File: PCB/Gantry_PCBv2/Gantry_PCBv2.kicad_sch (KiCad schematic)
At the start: 64 parts, among them J1 Conn_01x14, J10 B2B-XH-A_LF__SN_, J11 B2B-XH-A_LF__SN_, J12 B2B-XH-A_LF__SN_, J13 Conn_01x03_Pin, J14 USB_C_Receptacle_USB2.0_16P, J17 B2B-XH-A_LF__SN_, J2 Conn_01x14, J3 Conn_01x10, J4 Screw_Terminal_01x02, J5 DCJ200-10-A-XX-X_REVA, J6 Conn_01x04_Pin, J7 Conn_01x04_Pin, J8 Conn_01x04_Pin, J9 Conn_01x04_Pin, Q1 SS8050, Q2 SS8050, SW7 SW_0, SW8 SW_EN, U1 ESP32-WROOM-32E, U2 CH340C, U3 TB6612FNG H-bridge Motor Driv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, U4 LM2576S-5, U5 AMS1117-3.3, U6 DRV8825_STEPPER_MOTOR_DRIVER_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, U7 DRV8825_STEPPER_MOTOR_DRIVER_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, U8 DRV8825_STEPPER_MOTOR_DRIVER_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, U9 DRV8825_STEPPER_MOTOR_DRIVER_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

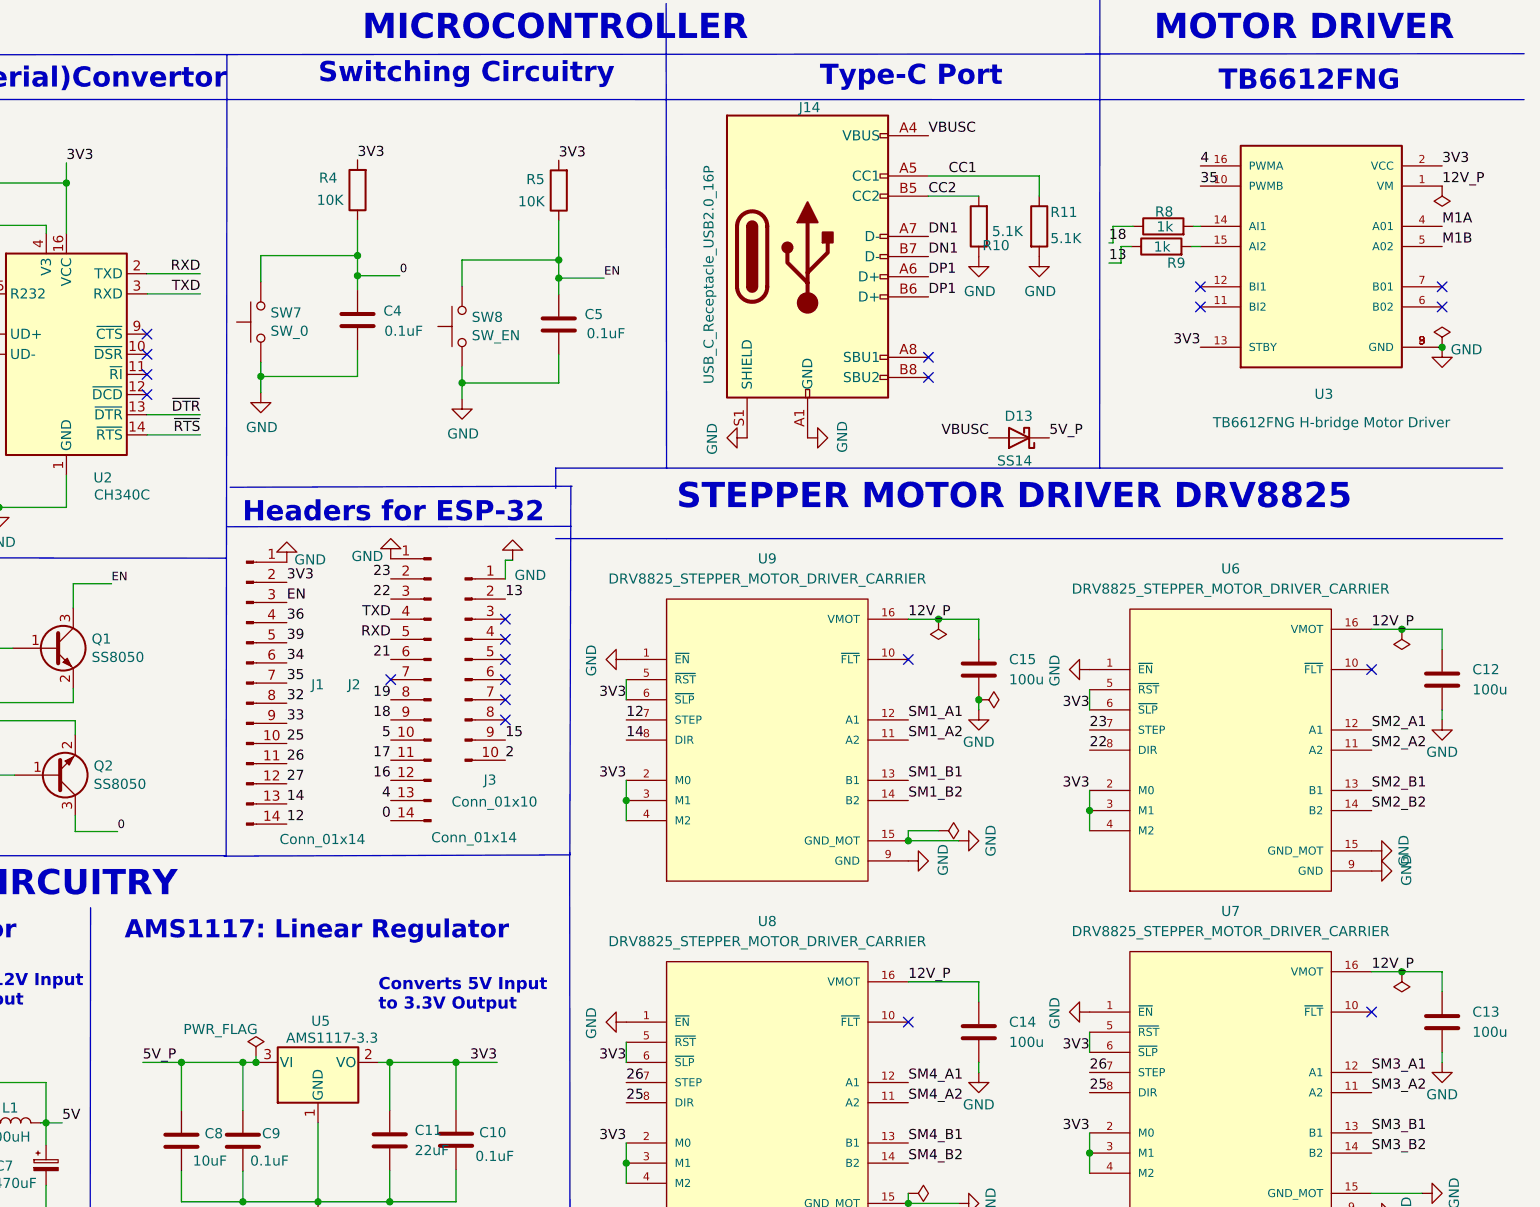
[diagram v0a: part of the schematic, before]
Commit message: final PCB Rounting without silkscreen
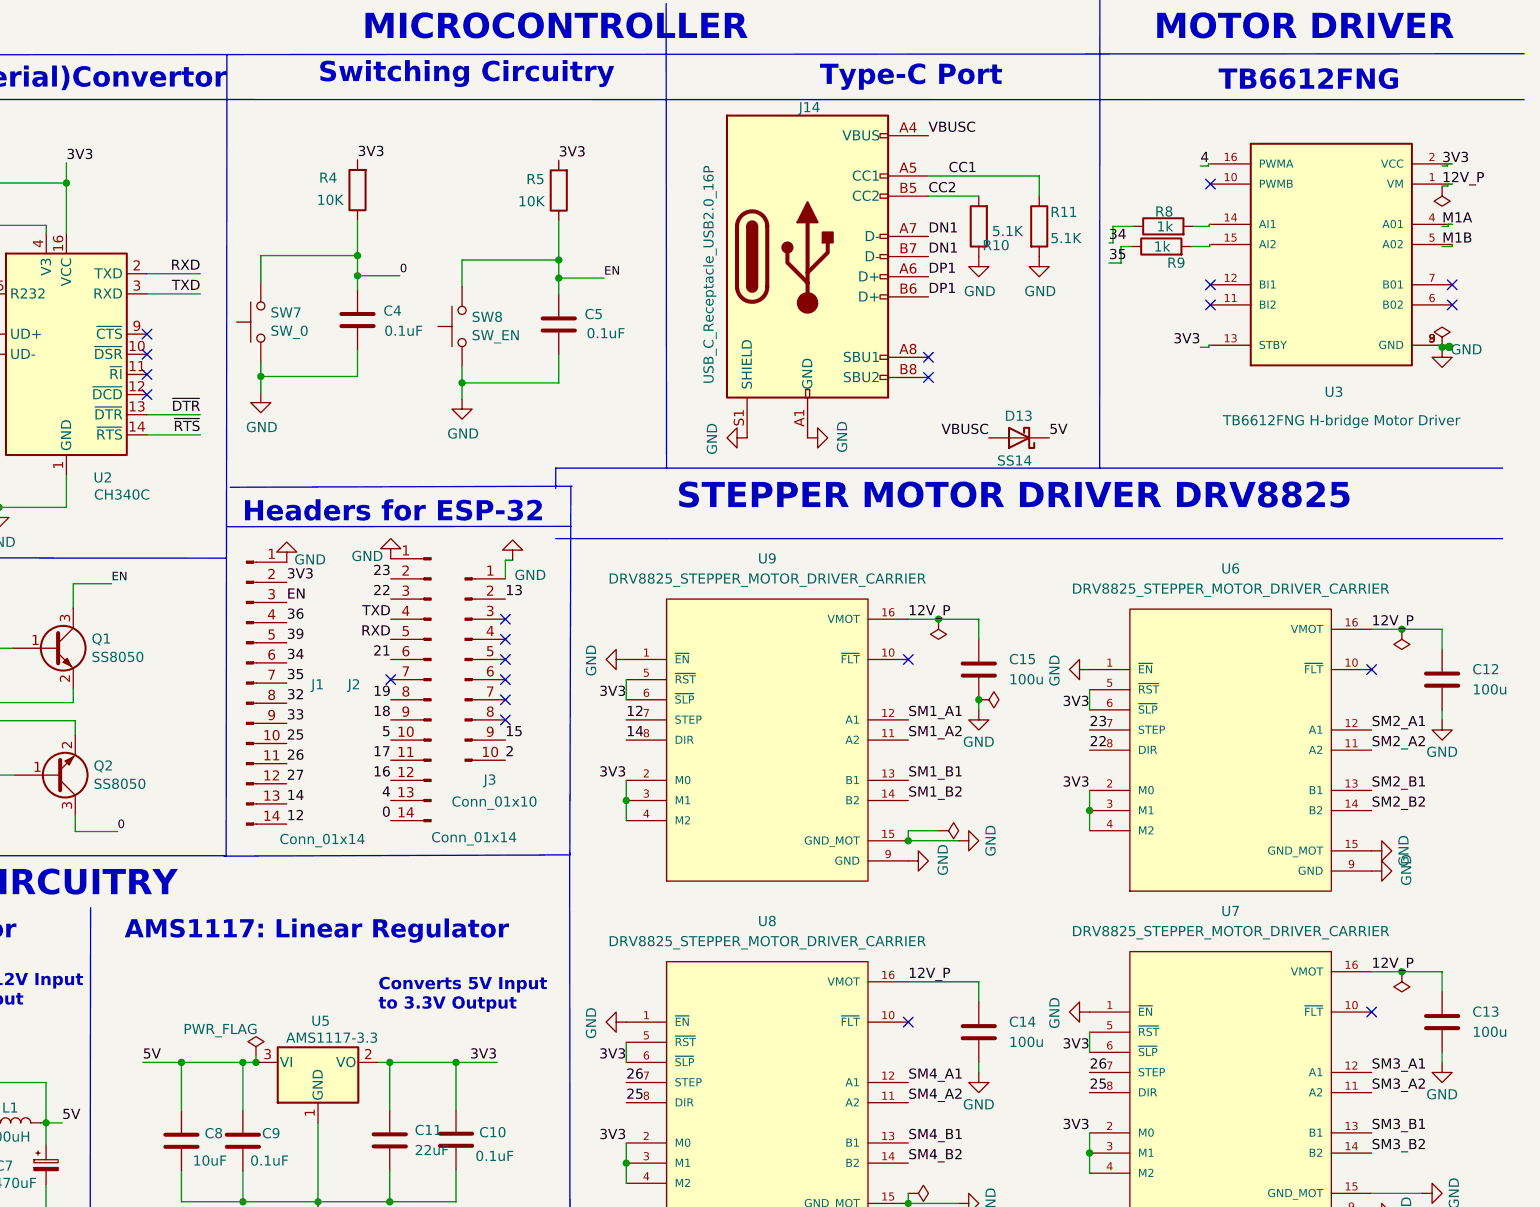
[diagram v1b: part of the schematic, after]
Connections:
- net 5V_P is gone; now on net 5V: C8.1, C9.1, D13.1 (K), U5.3 (VI)
- net 13: no longer R9.1
- net 18: no longer R8.1
- net 34: now also R8.1
- net 35: now also R9.1; no longer U3.10 (PWMB)
- no-connect marks 23 -> 24
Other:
- moved on the sheet: U3

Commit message: Schematic v3
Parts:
- removed C6: 100uF, Capacitor_SMD:CP_Elec_6.3x7.7, symbol Device:C_Polarized_Small
- removed C7: 470uF, Capacitor_SMD:CP_Elec_8x10, symbol Device:C_Polarized_Small
- removed D13: SS14, Diode_SMD:D_SMA, symbol Diode:1N5822
- removed D14: SS24, Diode_SMD:D_SMA, symbol Diode:1N5822
- removed D15: SS34, Diode_SMD:D_SMB, symbol Diode:1N5822
- removed J13: Conn_01x03_Pin, Connector_JST:JST_EH_B3B-EH-A_1x03_P2.50mm_Vertical, symbol Connector:Conn_01x03_Pin
- removed R10, R11: 5.1K, Resistor_SMD:R_0805_2012Metric, symbol ESP32-S2-rescue:R-Device
- removed U4: LM2576S-5, Package_TO_SOT_SMD:TO-263-5_TabPin3, symbol Regulator_Switching:LM2576S-5
- removed U5: AMS1117-3.3, Package_TO_SOT_SMD:SOT-223-3_TabPin2, symbol Regulator_Linear:AMS1117-3.3
- added C16, C25: 100n, Capacitor_SMD:CP_Elec_6.3x7.7, symbol Device:C
- added C17, C19, C20: 100nF, symbol Device:C
- added C18, C23: 1uF, Capacitor_SMD:C_0805_2012Metric, symbol Device:C
- added C21: 22uF, Capacitor_SMD:C_0805_2012Metric, symbol Device:C
- added C22: 0.1uF, Capacitor_SMD:C_0805_2012Metric, symbol Device:C
- added C24: 4.7uF, Capacitor_SMD:C_0805_2012Metric, symbol Device:C
- added C6: 10uF, Capacitor_SMD:C_0805_2012Metric, symbol Device:C
- added C6: 150pF, Capacitor_SMD:C_0805_2012Metric, symbol Device:C
- added C7: 100nF, Capacitor_SMD:C_0805_2012Metric, symbol Device:C
- added C7: NS, Capacitor_SMD:C_0805_2012Metric, symbol Device:C
- added D10, D11, D12, D17, D3, D9: Y_LED, symbol Device:LED
- added D13: R_LED, symbol Device:LED
- added D14: G_LED, symbol Device:LED
- added D15, D16: B_LED, symbol Device:LED
- added D4: SP0503BAHT, Package_TO_SOT_SMD:SOT-143, symbol Power_Protection:SP0503BAHT
- added D5: D_Schottky, Diode_SMD:D_SMA_Handsoldering, symbol Device:D_Schottky
- added D6, D8: SS14, Diode_SMD:D_SMA, symbol Diode:1N5822
- added D7: SS34, Diode_SMD:D_SMB, symbol Diode:1N5822
- added D7, D8: LED, LED_SMD:LED_0603_1608Metric_Pad1.05x0.95mm_HandSolder, symbol Device:LED_Small
- added F1: Polyfuse, symbol Device:Polyfuse
- added F2: 3A, Fuse:Fuse_Littelfuse-LVR100, symbol Device:Fuse
- added F2: 1A, Fuse:Fuse_Littelfuse-LVR100, symbol Device:Fuse
- added J15: Conn_01x03_Pin, Connector_JST:JST_EH_B3B-EH-A_1x03_P2.50mm_Vertical, symbol Connector:Conn_01x03_Pin
- added Q3: NMOS, symbol Simulation_SPICE:NMOS
- added R10, R11: 5.1K, Resistor_SMD:R_0805_2012Metric_Pad1.20x1.40mm_HandSolder, symbol Device:R
- added R12, R25, R26, R27, R28, R33: 600, Resistor_SMD:R_0805_2012Metric, symbol ESP32-S2-rescue:R-Device
- added R13, R24, R34, R35, R36, R37, R38, R39: 100, Resistor_SMD:R_0603_1608Metric, symbol Device:R
- added R14, R16, R6: 1K, symbol Device:R
- added R15, R17, R7: 10K, symbol Device:R
- added R18, R20, R21: 100k, Resistor_SMD:R_0805_2012Metric_Pad1.20x1.40mm_HandSolder, symbol Device:R
- added R19: 24.9k, Resistor_SMD:R_0805_2012Metric_Pad1.20x1.40mm_HandSolder, symbol Device:R
- added R22: 210k, Resistor_SMD:R_0805_2012Metric_Pad1.20x1.40mm_HandSolder, symbol Device:R
- added R23: 40.2k, Resistor_SMD:R_0805_2012Metric_Pad1.20x1.40mm_HandSolder, symbol Device:R
- added R29: 4.7k, Resistor_SMD:R_0805_2012Metric, symbol ESP32-S2-rescue:R-Device
- added R30: 1.5k, Resistor_SMD:R_0805_2012Metric, symbol ESP32-S2-rescue:R-Device
- added R31, R32: 150, Resistor_SMD:R_0805_2012Metric, symbol ESP32-S2-rescue:R-Device
- added R40: 10k, symbol Device:R_Variable
- added R49: 330, Resistor_SMD:R_0603_1608Metric_Pad0.98x0.95mm_HandSolder, symbol Device:R_Small
- added R50: 1.2k, Resistor_SMD:R_0805_2012Metric_Pad1.20x1.40mm_HandSolder, symbol Device:R_Small
- added TH1: 10k, symbol Device:Thermistor_NTC
- added TP1, TP2, TP3, TP4, TP5, TP6, TP7, TP8: TP, symbol Connector:TestPoint
- added U10: TLV75733PDBV, Package_TO_SOT_SMD:SOT-23-5, symbol Regulator_Linear:TLV75733PDBV
- added U11, U5: 74HC245, symbol 74xx:74HC245
- added U4: MP1584, Package_SO:SOIC-8-1EP_3.9x4.9mm_P1.27mm_EP2.41x3.3mm, symbol Regulator_Controller:UC3842_SOIC8
- C10: value 0.1uF -> 470u; footprint Capacitor_SMD:C_0805_2012Metric -> Capacitor_SMD:CP_Elec_6.3x7.7
- C11: value 22uF -> 100n; footprint Capacitor_SMD:C_0805_2012Metric -> Capacitor_SMD:CP_Elec_6.3x7.7
- C12, C14, C15: value 100u -> 470u
- C13: value 100u -> 100n
- C8: value 10uF -> 100n; footprint Capacitor_SMD:C_0805_2012Metric -> Capacitor_SMD:CP_Elec_6.3x7.7
- C9: value 0.1uF -> 100n; footprint Capacitor_SMD:C_0805_2012Metric -> Capacitor_SMD:CP_Elec_6.3x7.7
- J14: footprint Connector_USB:USB_C_Receptacle_HRO_TYPE-C-31-M-12 -> Connector_USB:USB_C_Receptacle_GCT_USB4105-xx-A_16P_TopMnt_Horizontal
- L1: value 100uH -> 15uH; footprint Inductor_SMD:L_10.4x10.4_H4.8 -> Inductor_SMD:L_Sunlord_MWSA0603S
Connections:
- net 12: now also U5.6 (A4); no longer U9.7 (STEP)
- net 12V: now also D7.2 (A)
- net 12V_P: now also J15.2 (Pin_2); no longer C12.1, C13.1, C14.1, C15.1, U6.16 (VMOT), U7.16 (VMOT), U8.16 (VMOT), U9.16 (VMOT)
- net 14: now also U5.7 (A5); no longer U9.8 (DIR)
- net 15: now also U11.2 (A0); no longer J10.1
- net 18: now also U11.4 (A2); no longer J12.1
- net 19: now also U11.3 (A1); no longer J11.1
- net 22: now also U5.3 (A1); no longer U6.8 (DIR)
- net 23: now also U5.2 (A0); no longer U6.7 (STEP)
- net 25: now also U5.5 (A3); no longer U7.8 (DIR), U8.8 (DIR)
- net 26: now also U5.4 (A2); no longer U7.7 (STEP), U8.7 (STEP)
- net 3V3: now also C23.1, C24.1, R31.2, R32.2, U10.5 (OUT), U11.1 (A->B), U5.1 (A->B); no longer C10.1, C11.1
- net 5V: now also C21.1, D8.2 (A), R22.1; no longer C8.1, C9.1
- net DN1: no longer J14.A7 (D-), J14.B7 (D-)
- net DP1: no longer J14.A6 (D+), J14.B6 (D+)
- net GND: now also C16.2, C17.2, C18.2, C19.2, C20.2, C21.2, C22.2, C23.2, C24.2, C25.2, C6.2, C7.2, D10.1 (K), D11.1 (K), D12.1 (K), D13.1 (K), D14.1 (K), D15.1 (K), D17.1 (K), D3.1 (K), D4.1 (A), D5.2 (A), D9.1 (K), Q3.3 (S), R10.2, R11.2, R19.2, R20.2, R21.2, R23.2, R40.2, R49.1, R50.1, U10.2 (GND), U11.10 (GND), U11.19 (CE), U4.5 (GND), U5.10 (GND), U5.19 (CE)
- net at L1.1: now also C7.2, D5.1 (K), U4.1 (SW)
- net CC1: no longer names the net of J14.A5 (CC1)
- net CC1: now also R10.1
- net CC2: no longer names the net of J14.B5 (CC2)
- net CC2: now also R11.1
- net VBUSC renamed VBUS
- net VBUS: now also D4.4 (K), D6.2 (A)
- new net: C19.1, J11.1, R14.2, R15.1
- new net: D17.2 (A), R28.1
- new net: C17.1, J10.1, R6.2, R7.1
- new net: D9.2 (A), R12.1
- new net: D7.1 (K), F2.1
- new net: D6.1 (K), F1.2
- new net: C8.1, U5.20 (VCC)
- new net: R37.2, U8.8 (DIR)
- new net: D15.2 (A), R31.1
- new net: D8.1 (K), F2.1
- new net: R34.2, U6.7 (STEP)
- new net: D8.1 (K), R50.2
- new net: D14.2 (A), R30.1
- new net: R36.2, U8.7 (STEP)
- new net: C7.1, U4.8 (BST)
- new net: C25.1, U11.20 (VCC)
- new net: D16.2 (A), R32.1
- new net: D11.2 (A), R26.1
- new net: D10.2 (A), R25.1
- new net: C20.1, J12.1, R16.2, R17.1
- new net: D12.2 (A), R27.1
- new net: C6.2, R21.1
- new net: J15.3 (Pin_3), Q3.1 (D), TH1.1
- new net: D13.2 (A), R29.1
- new net: C6.1, C7.1, U4.3 (COMP)
- new net: R20.1, U4.6 (FREQ)
- new net: R39.2, U7.8 (DIR)
- new net: R35.2, U6.8 (DIR)
- new net: Q3.2 (G), R40.1, TH1.2
- new net: D3.2 (A), R33.1
- new net: R38.2, U7.7 (STEP)
- new net: D7.1 (K), R49.2
- new net: R13.2, U9.7 (STEP)
- new net: R24.2, U9.8 (DIR)
- new net 12V_R: C10.1, C11.1, C12.1, C13.1, C14.1, C15.1, C16.1, C6.1, C9.1, D8.2 (A), F2.2, R18.1, R29.2, TP7.1, U4.7 (VIN), U6.16 (VMOT), U7.16 (VMOT), U8.16 (VMOT), U9.16 (VMOT)
- new net 3.3V: R15.2, R17.2, R7.2
- new net 5V_R: C18.1, C22.1, D7.2 (A), F1.1, F2.2, R30.2, TP8.1, U10.1 (IN)
- new net Any GPIO: D16.1 (K)
- new net D+: D4.2 (K), J14.A6 (D+), J14.B6 (D+)
- new net D-: D4.3 (K), J14.A7 (D-), J14.B7 (D-)
- new net EN_SR: R18.2, R19.1, U4.2 (EN)
- new net FB: R22.2, R23.1, U4.4 (FB)
- new net LS_1: R6.1, U11.18 (B0)
- new net LS_2: R14.1, U11.17 (B1)
- new net LS_3: R16.1, U11.16 (B2)
- new net M1_D: R12.2, R24.1, TP2.1, U5.13 (B5)
- new net M1_S: R13.1, R33.2, TP1.1, U5.14 (B4)
- new net M2_D: R26.2, R35.1, TP4.1, U5.17 (B1)
- new net M2_S: R25.2, R34.1, TP3.1, U5.18 (B0)
- new net M3/4_D: R28.2, R37.1, R39.1, TP6.1, U5.15 (B3)
- new net M3/4_S: R27.2, R36.1, R38.1, TP5.1, U5.16 (B2)
- no-connect marks 24 -> 38
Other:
- note added: "74HC245"
- note added: "BUFFER IC"
- note added: "Diagnostic LEDs & Test Points"
- note added: "MP1584 Buck Convertor"
- note added: "Serial Boot"
- note added: "TLV75733: LDO Regulator"
- note added: "To Be Confirmed"
- note removed: "AMS1117: Linear Regulator"
- note removed: "LM2576: Buck Regulator"
- moved on the sheet: C15, H1, H2, H3, H4, H5, H6, H7, H8, J10, J11, J12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
